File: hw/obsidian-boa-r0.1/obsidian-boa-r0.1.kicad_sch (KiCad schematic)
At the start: 87 parts, among them J1 USB_C, J2 PROG, P0 0, P1 1, P10 10, P11 11, P12 12, P13 13, P14 14, P15 15, P16 16, P17 17, P18 18, P19 19, P2 2, P20 20, P21 21, P22 22, P23 23, P24 GND, P25 GND, P26 GND, P27 3V3, P28 3V3, P29 VIN, P3 3, P30 CDONE, P31 CRESET, P32 UP, P33 UP, P34 UP, P35 UP, P4 4, P5 5, P6 6, P7 7, P8 8, P9 9, SW1 TACT, U1 USBLC6-2, U2 W25Q32JVSS, U3 ESP32-S2, U4 W25Q32JVSS, U5 TPS62290, Y1 40MHz

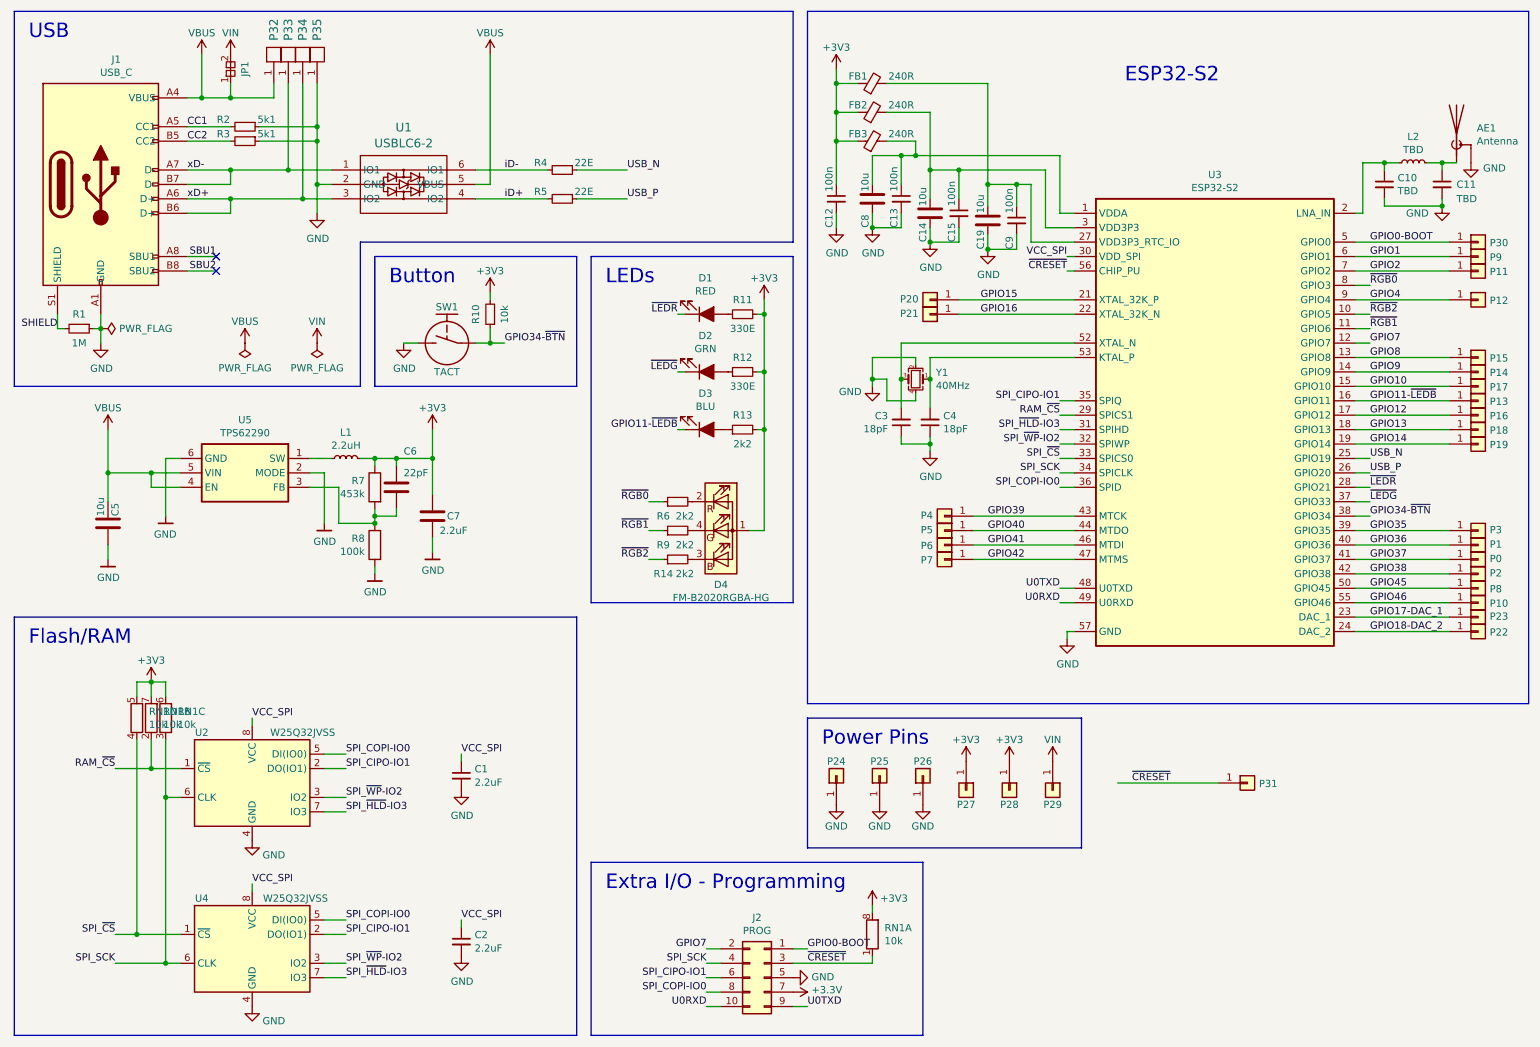
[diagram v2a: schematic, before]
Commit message: hw: Update PSRAM/FLASH part numbers
 - Regenerate schematic
 - Add generated BOM
#6
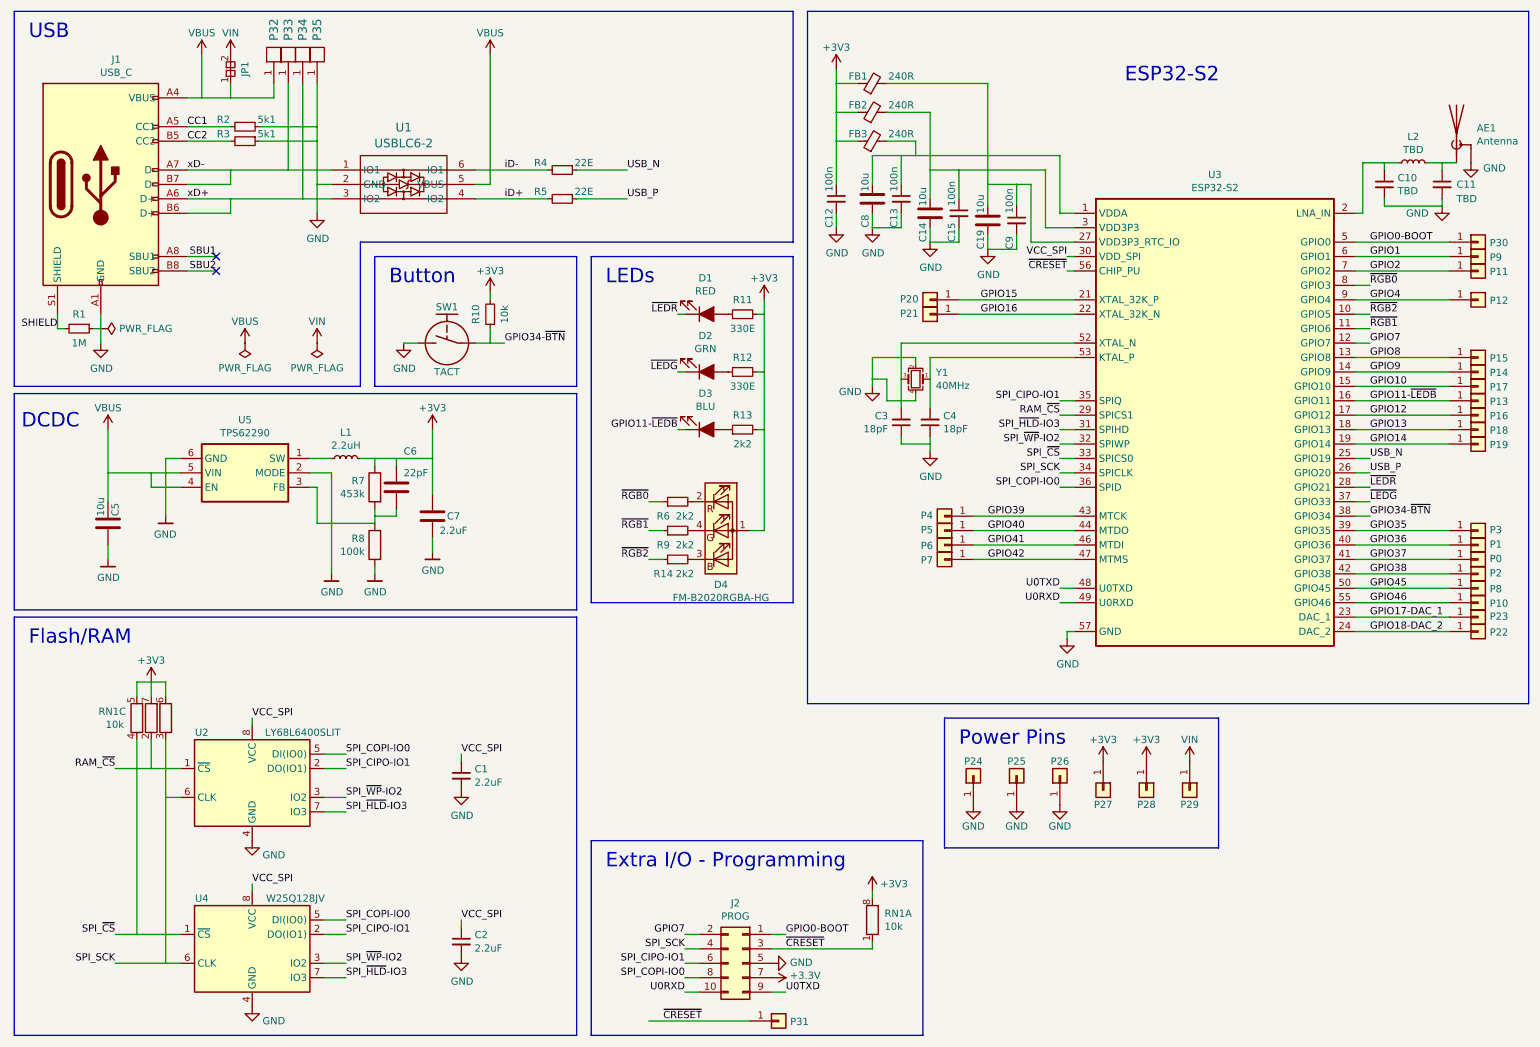
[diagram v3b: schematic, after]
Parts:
- U2: value W25Q32JVSS -> LY68L6400SLIT
- U4: value W25Q32JVSS -> W25Q128JV
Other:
- note added: "DCDC"
- moved on the sheet: J2, P24, P25, P26, P27, P28, P29, P31, RN1A
